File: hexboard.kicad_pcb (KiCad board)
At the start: 2 copper layers, 91.3 x 105.4 mm, 34 parts, among them J1 USB_C_Receptacle_USB2.0_16P, J2 USB_A, J3 Conn_01x20, J4 Conn_01x20, SW1 SW_Push, SW2 SW_Push, U1 RP2040, U2 MCP1700x-330xxTT, U3 W25Q16JVSS, Y1 Crystal_GND23_Small

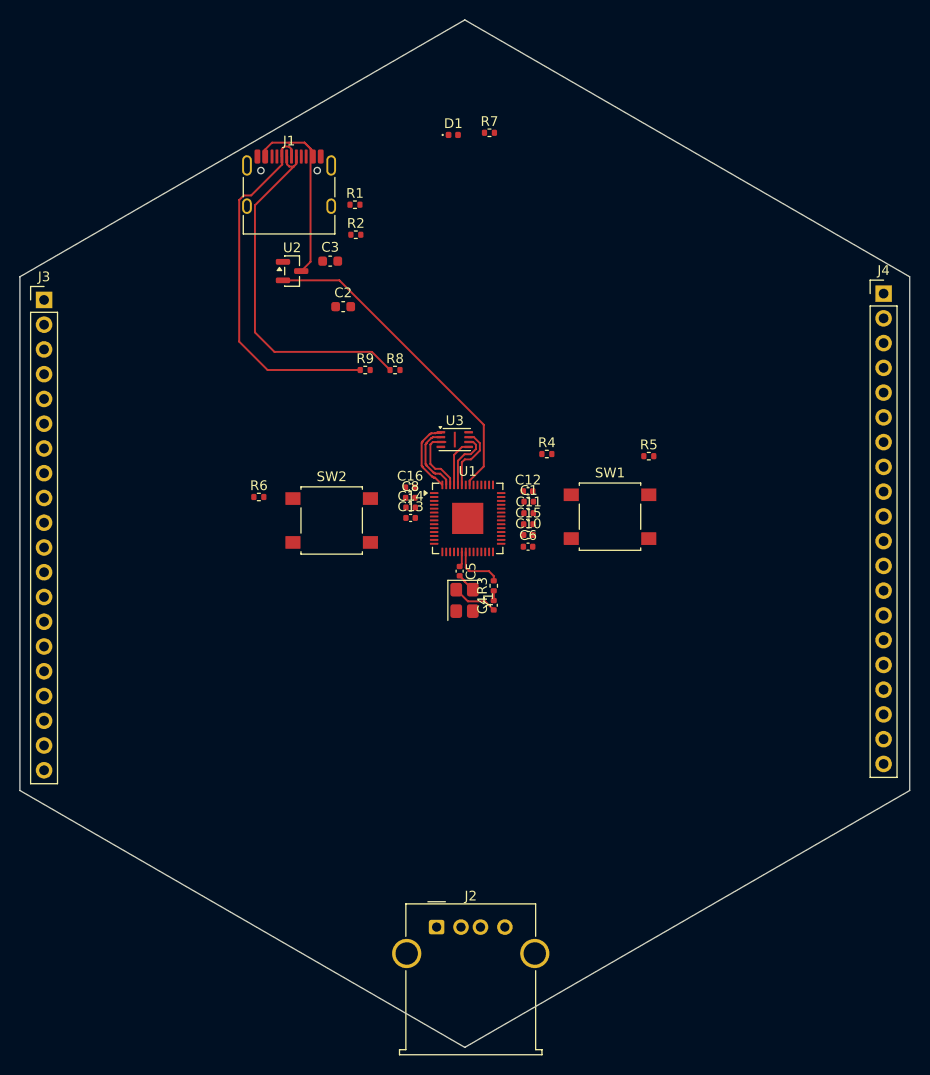
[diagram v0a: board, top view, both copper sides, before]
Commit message: started routing headers
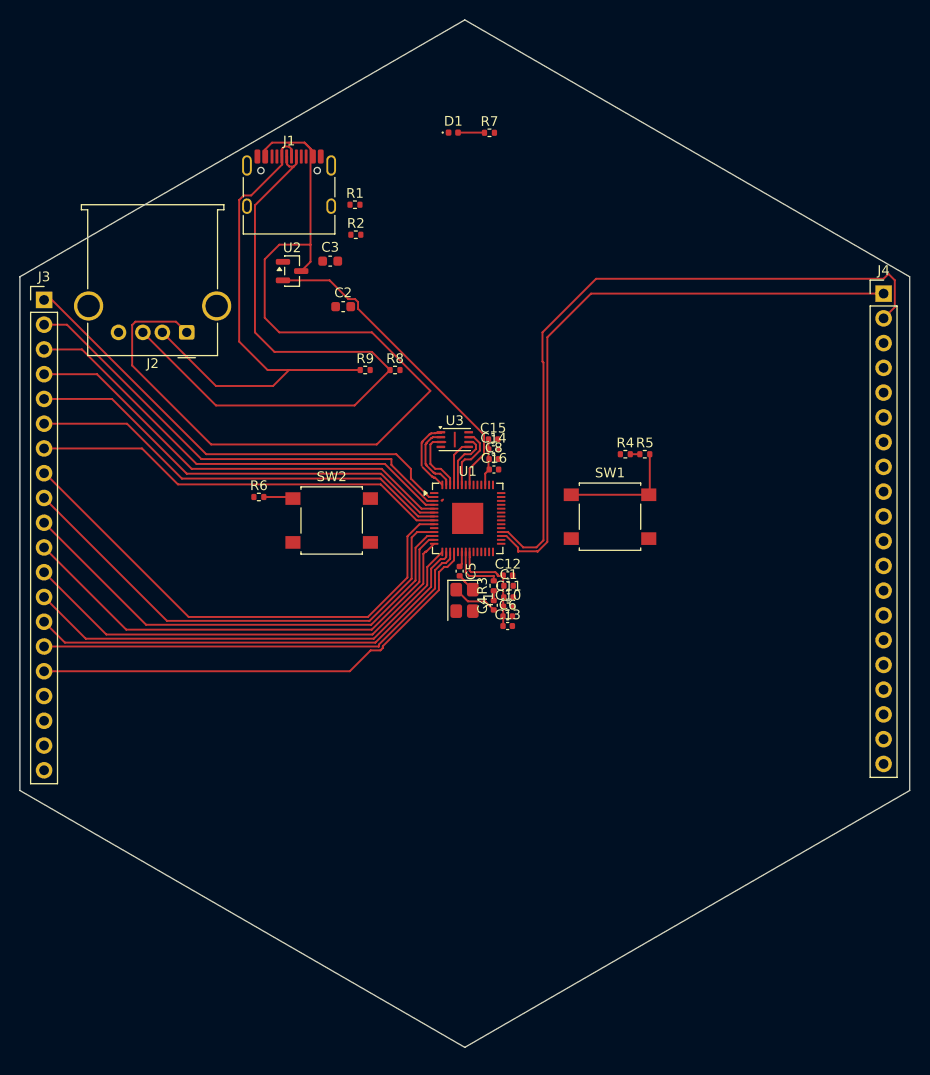
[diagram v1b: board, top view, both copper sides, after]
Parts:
- moved J2 66.2 mm to (100.5, 97.0), turned to 180 degrees
- moved C13 14.9 mm to (133.4, 127.1)
- moved C14 10.4 mm to (132.0, 109.0)
- moved C8 9.44 mm to (132.0, 110.0)
- moved C15 9.43 mm to (131.9, 108.0)
- moved C11 8.87 mm to (133.5, 124.2)
- moved C12 8.87 mm to (133.4, 121.9)
- moved C1 8.87 mm to (133.5, 123.0)
- moved C16 8.79 mm to (132.0, 111.1)
- moved R4 8.05 mm to (145.5, 109.5)
- moved C10 7.63 mm to (133.5, 125.1)
- moved C6 7.44 mm to (133.4, 126.1)
- moved R5 0.46 mm to (147.5, 109.5)
- moved D1 0.24 mm to (127.8, 76.5)
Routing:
- net VBUS: track 20.7 -> 98.7 mm
- net Net-(J4-Pin_2): track 0.00 -> 70.0 mm
- net Net-(J4-Pin_1): track 0.00 -> 63.4 mm
- net Net-(J3-Pin_8): track 0.00 -> 52.6 mm
- net Net-(J3-Pin_9): track 0.00 -> 51.5 mm
- net Net-(J3-Pin_10): track 0.00 -> 50.1 mm
- net Net-(J3-Pin_11): track 0.00 -> 49.3 mm
- net Net-(J3-Pin_1): track 0.00 -> 49.0 mm
- net Net-(J3-Pin_16): track 0.00 -> 48.8 mm
- net Net-(J3-Pin_12): track 0.00 -> 48.3 mm
- net Net-(J3-Pin_2): track 0.00 -> 47.9 mm
- net Net-(J3-Pin_13): track 0.00 -> 47.4 mm
- net Net-(J3-Pin_14): track 0.00 -> 47.4 mm
- net Net-(J3-Pin_15): track 0.00 -> 47.3 mm
- net Net-(J3-Pin_3): track 0.00 -> 46.6 mm
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
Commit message: added more header power lines
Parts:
- moved J4 48.6 mm to (172.0, 141.6), turned to 180 degrees
- moved SW1 4.07 mm to (148.0, 115.9)
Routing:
- net Net-(J4-Pin_6): track 0.00 -> 62.7 mm
- net Net-(J4-Pin_5): track 0.00 -> 61.9 mm
- net Net-(J4-Pin_4): track 0.00 -> 61.1 mm
- net Net-(J4-Pin_3): track 0.00 -> 60.4 mm
- net Net-(J4-Pin_2): track 70.0 -> 59.4 mm
- net Net-(J4-Pin_1): track 63.4 -> 58.7 mm
- net Net-(R5-Pad2): track 12.2 -> 16.0 mm

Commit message: more power lines
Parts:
- moved J4 2.03 mm to (170.5, 143.0)
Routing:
- net Net-(J4-Pin_11): track 0.00 -> 65.2 mm
- net Net-(J4-Pin_10): track 0.00 -> 64.6 mm
- net Net-(J4-Pin_9): track 0.00 -> 63.8 mm
- net Net-(J4-Pin_8): track 0.00 -> 62.9 mm
- net Net-(J4-Pin_6): track 62.7 -> 60.7 mm
- net Net-(J4-Pin_5): track 61.9 -> 59.9 mm
- net Net-(J4-Pin_4): track 61.1 -> 59.1 mm
- net Net-(J4-Pin_2): track 59.4 -> 57.4 mm
- net Net-(J4-Pin_3): track 60.4 -> 58.4 mm
- net Net-(J4-Pin_1): track 58.7 -> 57.8 mm

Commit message: more routing
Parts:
- moved J4 0.50 mm to (170.0, 143.0)
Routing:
- net /RUN: track 3.05 -> 104.0 mm
- net /SWCLK: track 0.00 -> 96.4 mm
- net Net-(J4-Pin_2): track 57.4 -> 56.8 mm
- net GND: track 0.10 -> 0.64 mm

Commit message: finished routing
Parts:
- moved C4 5.95 mm to (129.1, 130.2)
- moved R3 5.95 mm to (129.1, 128.2)
- moved Y1 4.96 mm to (126.7, 128.9)
- moved C13 4.31 mm to (131.0, 130.7)
- moved C6 4.07 mm to (131.0, 129.4)
- moved C5 4.00 mm to (127.6, 125.4), turned to 90 degrees
- moved C10 3.91 mm to (131.1, 128.2)
- moved C11 3.72 mm to (131.1, 127.0)
- moved C1 3.70 mm to (131.1, 125.8)
- moved C12 3.57 mm to (131.1, 124.6)
- moved C14 0.63 mm to (132.6, 109.0)
- moved C15 0.63 mm to (132.6, 108.0)
- moved C16 0.63 mm to (132.7, 111.1)
- moved C8 0.63 mm to (132.6, 110.0)
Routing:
- net +3V3: track 44.2 -> 189.4 mm, vias 0 -> 7
- net /SWDIO: track 0.00 -> 104.1 mm
- net VBUS: track 98.7 -> 169.2 mm
- net Net-(J3-Pin_20): track 0.00 -> 69.7 mm, vias 0 -> 2
- net Net-(J3-Pin_19): track 0.00 -> 66.7 mm, vias 0 -> 2
- net Net-(J3-Pin_18): track 0.00 -> 63.9 mm, vias 0 -> 2
- net Net-(J3-Pin_17): track 0.00 -> 61.8 mm, vias 0 -> 2
- net GND: track 0.64 -> 37.6 mm, vias 0 -> 7
- net +1V1: track 4.89 -> 38.0 mm, vias 0 -> 3
- net QSPI_SS: track 8.80 -> 32.5 mm, vias 0 -> 2
- net /RUN: track 104.0 -> 126.4 mm, vias 0 -> 2
- net /SWCLK: track 96.4 -> 114.4 mm
- net USB_DP_MCU: track 0.00 -> 17.3 mm, vias 0 -> 2
- net USB_DM_MCU: track 0.00 -> 17.1 mm, vias 0 -> 2
- net Net-(J1-CC1): track 0.00 -> 13.0 mm, vias 0 -> 2
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- added copper zone on B.Cu, net GND
- added copper zone on F.Cu, net GND

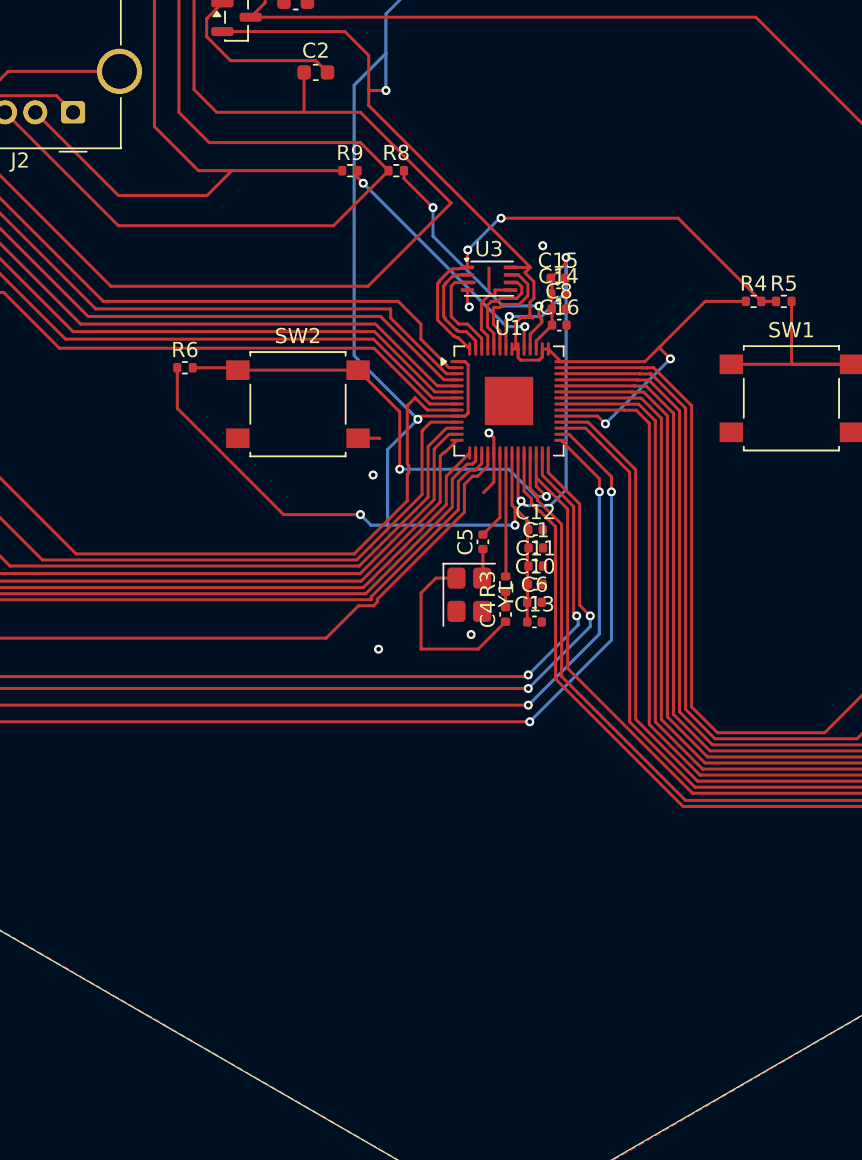
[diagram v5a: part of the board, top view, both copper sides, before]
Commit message: added hexagon design and handle on the front and started adding an oled header
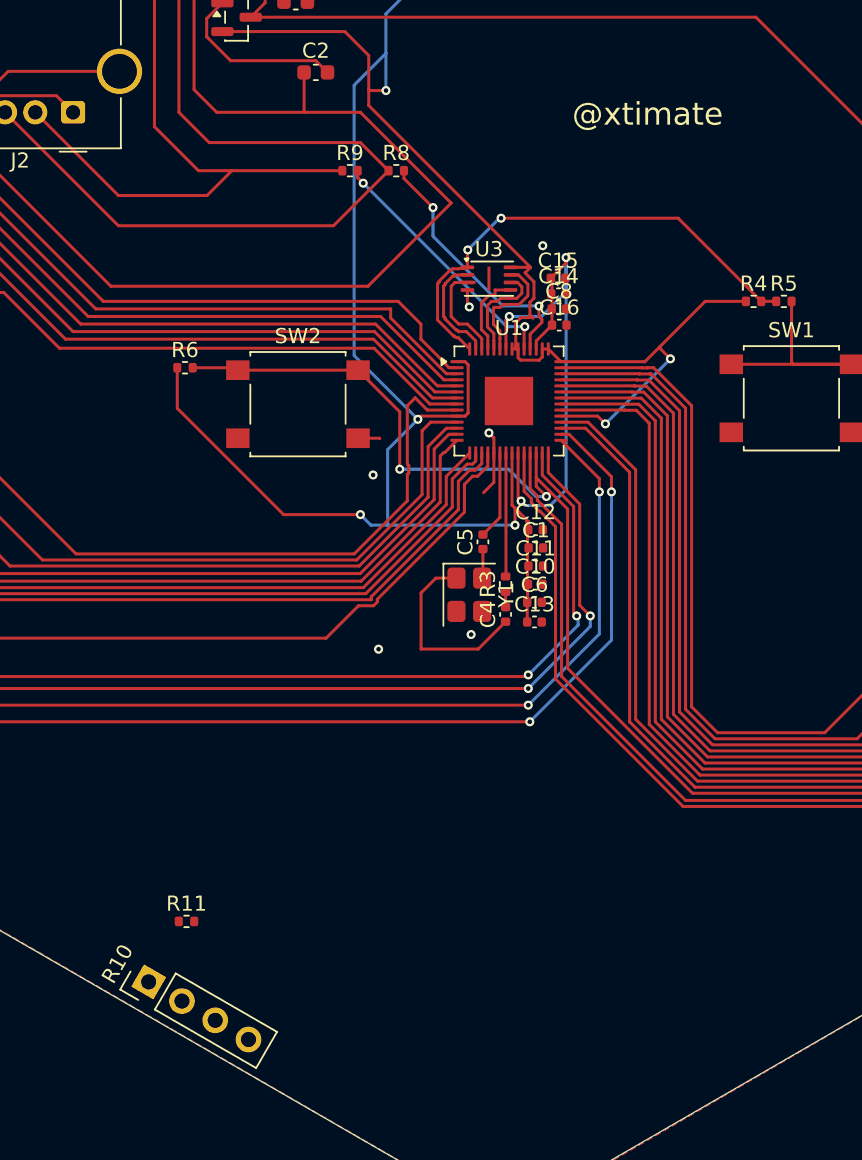
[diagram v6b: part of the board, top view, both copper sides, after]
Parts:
- added R10: 4.7K, Connector_PinHeader_2.54mm:PinHeader_1x04_P2.54mm_Vertical, F.Cu at (105.5, 154.5)
- added R11: 4.7K, Resistor_SMD:R_0402_1005Metric, F.Cu at (108.0, 150.5)
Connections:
- net Net-(J3-Pin_5) renamed I2C_SDA
- net Net-(J3-Pin_6) renamed I2C_SCL
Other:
- board text added: "@xtimate"

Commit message: added design on back and added a few more things
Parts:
- added C7: 0.1uF, Capacitor_SMD:C_0402_1005Metric, F.Cu at (123.1, 145.4)
- added D2: LED, LED_SMD:LED_0402_1005Metric, F.Cu at (127.9, 74.4)
- added D3: WS2812B, LED_SMD:LED_WS2812B_PLCC4_5.0x5.0mm_P3.2mm, F.Cu at (128.8, 147.0)
- added J5: Conn_01x04, Connector_PinHeader_2.54mm:PinHeader_1x04_P2.54mm_Vertical, F.Cu at (145.3, 77.2)
- added R12: 10K, Resistor_SMD:R_0402_1005Metric, F.Cu at (105.4, 113.9)
- added R13: 100 ohm, Resistor_SMD:R_0402_1005Metric, F.Cu at (131.4, 74.4)
- added SW3: SW_Push, Button_Switch_SMD:SW_SPST_B3S-1000, F.Cu at (101.8, 118.4)
- added TP1: TESTVBUS, TestPoint:TestPoint_Pad_1.0x1.0mm, F.Cu at (154.8, 82.4)
- added TP2: TEST_3V3, TestPoint:TestPoint_Pad_1.0x1.0mm, F.Cu at (149.7, 79.6)
- added TP3: TESTGND, TestPoint:TestPoint_Pad_1.0x1.0mm, F.Cu at (158.8, 84.9)
- added TP4: TESTSCL, TestPoint:TestPoint_Pad_1.0x1.0mm, F.Cu at (133.0, 69.2)
- added TP5: TESTSDA, TestPoint:TestPoint_Pad_1.0x1.0mm, F.Cu at (136.0, 71.0)
- added U4: TMP102xxDRL, Package_TO_SOT_SMD:SOT-563, F.Cu at (142.8, 84.3)
- R10: footprint Connector_PinHeader_2.54mm:PinHeader_1x04_P2.54mm_Vertical -> Resistor_SMD:R_0402_1005Metric
- U3: footprint Package_SON:Winbond_USON-8-1EP_3x2mm_P0.5mm_EP0.2x1.6mm -> Package_SO:SOIC-8_3.9x4.9mm_P1.27mm
- moved R10 83.9 mm to (139.3, 77.7)
- moved R11 79.1 mm to (136.2, 76.6), turned to 150 degrees
- moved C14 7.40 mm to (139.9, 107.8)
- moved C15 7.40 mm to (139.9, 106.8)
- moved C8 7.40 mm to (139.9, 108.8)
- moved C16 7.40 mm to (139.9, 109.9)
- moved J2 3.64 mm to (102.7, 94.1), turned to -150 degrees
- moved R6 2.73 mm to (109.5, 116.1), turned to 90 degrees
- moved SW1 0.56 mm to (147.6, 116.3)
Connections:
- net Net-(J3-Pin_7) renamed USR_BTN
- net Net-(J3-Pin_8) renamed USR_LED
- net Net-(J3-Pin_9) renamed RGB_DIN
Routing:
- net I2C_SCL: track 44.0 -> 115.4 mm, vias 0 -> 5
- net I2C_SDA: track 44.9 -> 108.8 mm, vias 0 -> 5
- net USR_LED: track 54.5 -> 107.5 mm, vias 0 -> 6
- net VBUS: track 169.2 -> 216.2 mm, vias 0 -> 4
- net +3V3: track 189.4 -> 226.9 mm, vias 7 -> 12
- net RGB_DIN: track 51.5 -> 85.8 mm, vias 0 -> 2
- net USB_DP_MCU: track 17.3 -> 43.8 mm
- net +1V1: track 38.0 -> 53.9 mm
- net USR_BTN: track 43.1 -> 57.9 mm
- net QSPI_SD0: track 5.71 -> 20.2 mm
- net QSPI_SCLK: track 6.96 -> 16.5 mm
- net USB_DM: track 53.9 -> 57.6 mm
- net Net-(D2-A): track 0.00 -> 2.50 mm
- net USB_DM_MCU: track 17.1 -> 19.2 mm
- net Net-(R5-Pad2): track 16.0 -> 14.0 mm
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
